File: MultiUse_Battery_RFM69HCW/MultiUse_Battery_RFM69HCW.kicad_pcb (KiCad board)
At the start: 2 copper layers, 49 x 26.5 mm, 16 parts, among them IC1 ATMEGA328P-AU, P1 CONN_01X02, P5 CONN_02X03, U2 AP111733, U3 RFM69HCW

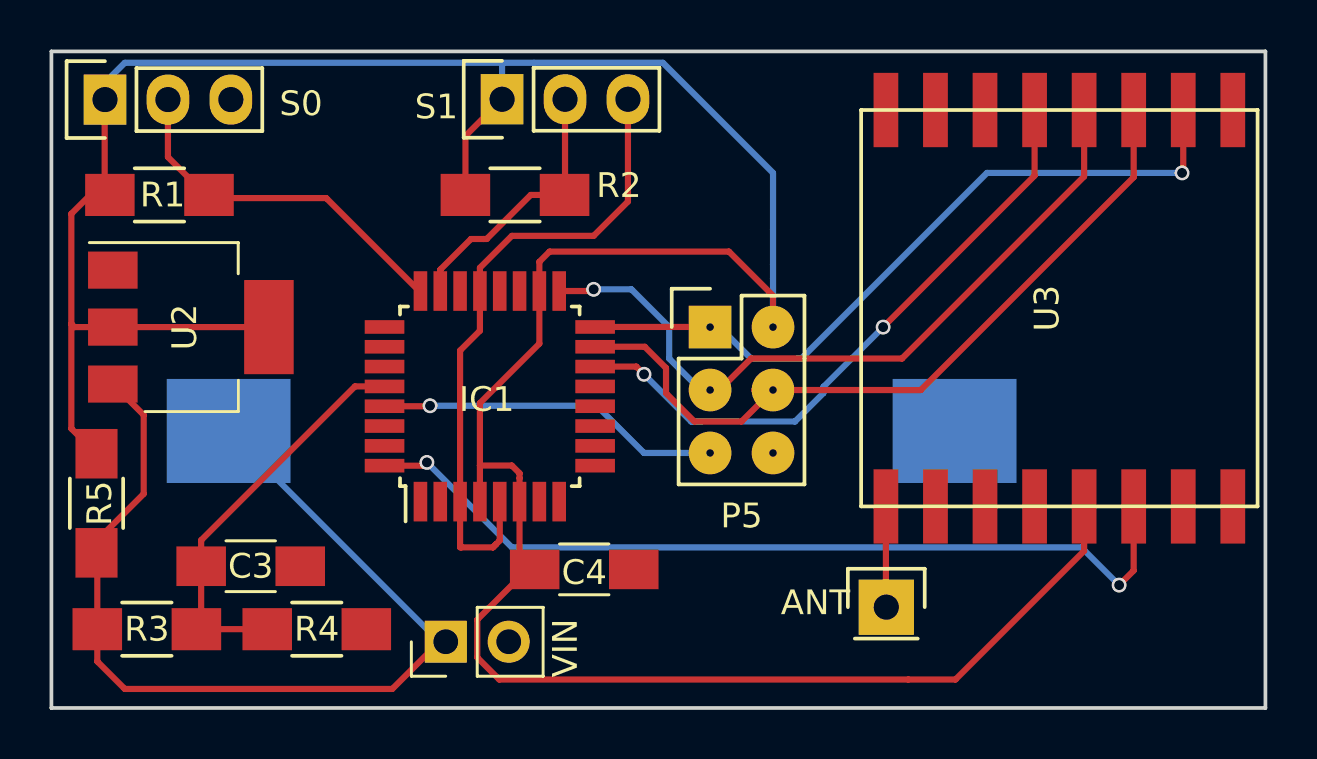
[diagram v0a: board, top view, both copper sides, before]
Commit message: Update to MultiUse_Battery_RFM69HCW (schematic + firmware) WIP of mySensors_Teleinfo
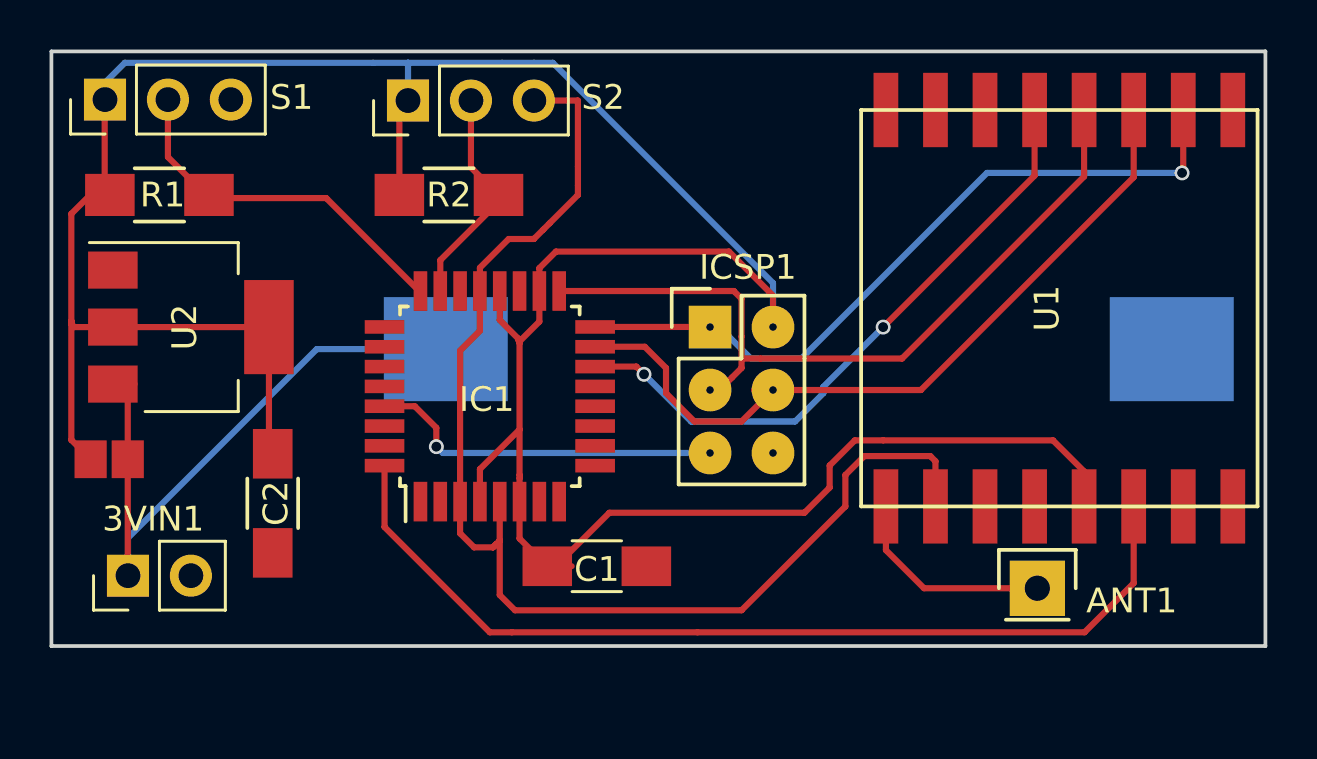
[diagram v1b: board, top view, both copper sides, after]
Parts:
- removed C3: 100nF, Capacitors_SMD:C_1206_HandSoldering
- removed R3: 10M, Resistors_SMD:R_1206_HandSoldering
- removed R4: 4.7M, Resistors_SMD:R_1206_HandSoldering
- removed R5: 0, Resistors_SMD:R_1206_HandSoldering
- removed S0: CONN_01X03, Pin_Headers:Pin_Header_Straight_1x03
- added ?: , MyLibrary:Jump, F.Cu at (84.6, 69.0)
- added C2: 10uF, Capacitors_SMD:C_1206_HandSoldering, F.Cu at (90.9, 70.7)
- added S2: CONN_01X03, Pin_Headers:Pin_Header_Straight_1x03_Pitch2.54mm, F.Cu at (96.4, 54.5)
- S1: footprint Pin_Headers:Pin_Header_Straight_1x03 -> Pin_Headers:Pin_Header_Straight_1x03_Pitch2.54mm
- moved S1 16.0 mm to (84.2, 54.4)
- moved 3VIN1 13.1 mm to (85.1, 73.7)
- moved P1 9.36 mm to (97.9, 64.5)
- moved ANT1 6.14 mm to (121.8, 74.2)
- moved R2 2.67 mm to (98.0, 58.3)
- moved C1 0.52 mm to (104.0, 73.3)
- renumbered VIN to 3VIN1, ANT to ANT1, C4 to C1, P5 to ICSP1, U3 to U1
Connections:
- IC1 pad 20: Net-(IC1-Pad20) -> /3V3
- S1 pad 2: /PC1 -> /PC0
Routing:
- net /GND: track 26.3 -> 52.1 mm
- net /VBAT: track 16.1 -> 0.00 mm
- net /VIN: track 40.0 -> 27.2 mm
- net /IRQ: track 35.2 -> 40.4 mm, vias 2 -> 0
- net Net-(ANT1-Pad1): track 4.07 -> 8.51 mm
- net /PC1: track 11.2 -> 9.17 mm
- net /3V3: track 128.9 -> 126.8 mm
- net /SCK: track 29.9 -> 31.9 mm, vias 1 -> 0
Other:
- board size 49 x 26.5 mm -> 49 x 24 mm
